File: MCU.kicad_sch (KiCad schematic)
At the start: 21 parts, among them U6 STM32F103RBTx, Y1 LFXTAL026380

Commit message: final version v2.1
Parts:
- C78, C79: value 100n -> 22p
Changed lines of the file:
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@@
       (effects (font (size 1.27 1.27)) (justify left))
     )
-    (property "Value" "100n" (id 1) (at 77.47 125.73 0)
+    (property "Value" "22p" (id 1) (at 77.47 125.73 0)
       (effects (font (size 1.27 1.27)) (justify left))
     )
@@
       (effects (font (size 1.27 1.27)) (justify left))
     )
-    (property "Value" "100n" (id 1) (at 93.98 125.73 0)
-      (effects (font (size 1.27 1.27)) (justify left))
-    )
+    (property "Value" "22p" (id 1) (at 93.98 125.73 0)
+      (effects (font (size 1.27 1.27)) (justify left))
+    )

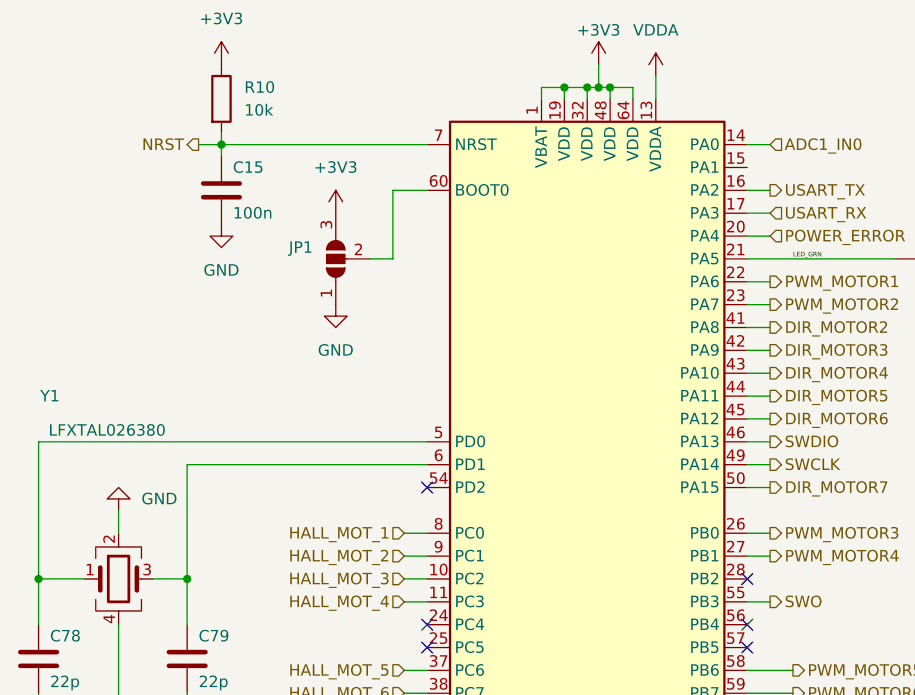
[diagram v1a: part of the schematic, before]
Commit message: updated footprints on board and sgematics
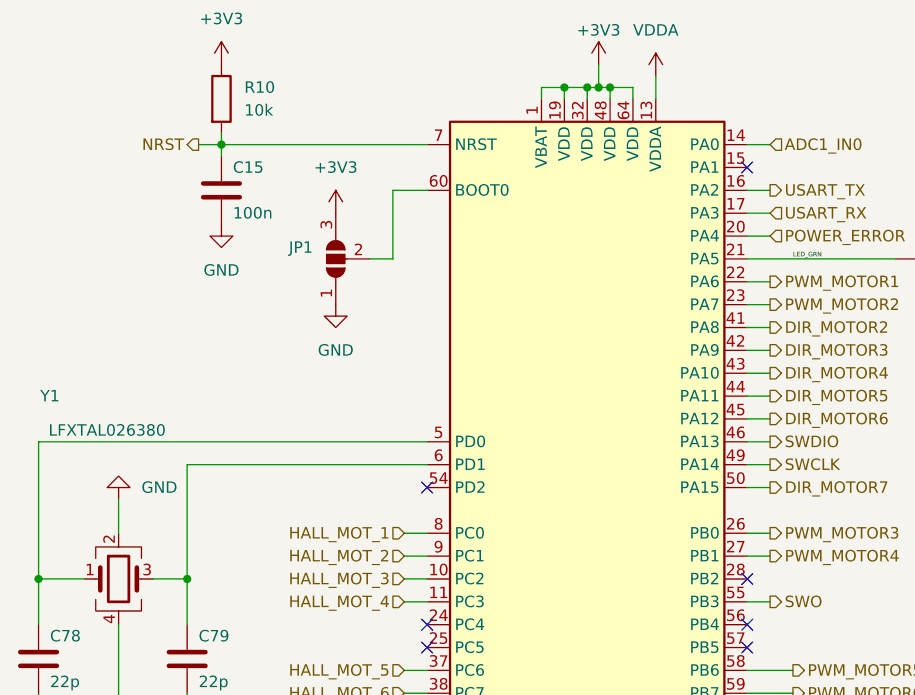
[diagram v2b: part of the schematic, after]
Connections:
- net VDDA: no longer names the net of C80.1, C81.1, FB1.2
- net VDDA: no longer U6.13 (VDDA)
- no-connect marks 13 -> 14
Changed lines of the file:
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@@
   (no_connect (at 154.94 121.92))
   (no_connect (at 154.94 132.08))
+  (no_connect (at 154.94 68.58))
   (no_connect (at 119.38 104.14))
   (wire (pts (xy 85.09 119.38) (xy 85.09 129.54))
@@
     (stroke (width 0) (type default) (color 0 0 0 0))
   )
-  (wire (pts (xy 85.09 106.68) (xy 85.09 109.22))
+  (wire (pts (xy 85.09 105.41) (xy 85.09 109.22))
     (stroke (width 0) (type default) (color 0 0 0 0))
   )
@@
     (pin "9")
   )
-  (symbol (lib_id "power:GND") (at 85.09 106.68 180) (unit 1)
-    (in_bom yes) (on_board yes) (fields_autoplaced)
-    (property "Reference" "#PWR030" (id 0) (at 85.09 100.33 0)
-      (effects (font (size 1.27 1.27)) hide)
-    )
-    (property "Value" "GND" (id 1) (at 87.63 105.4099 0)
+  (symbol (lib_id "power:GND") (at 85.09 105.41 180) (unit 1)
+    (in_bom yes) (on_board yes) (fields_autoplaced)
+    (property "Reference" "#PWR030" (id 0) (at 85.09 99.06 0)
+      (effects (font (size 1.27 1.27)) hide)
+    )
+    (property "Value" "GND" (id 1) (at 87.63 104.1399 0)
       (effects (font (size 1.27 1.27)) (justify right))
     )
-    (property "Footprint" "" (id 2) (at 85.09 106.68 0)
-      (effects (font (size 1.27 1.27)) hide)
-    )
-    (property "Datasheet" "" (id 3) (at 85.09 106.68 0)
+    (property "Footprint" "" (id 2) (at 85.09 105.41 0)
+      (effects (font (size 1.27 1.27)) hide)
+    )
+    (property "Datasheet" "" (id 3) (at 85.09 105.41 0)
       (effects (font (size 1.27 1.27)) hide)
     )
@@
     (pin "2")
   )
-  (symbol (lib_id "power:VDDA") (at 144.78 58.42 0) (unit 1)
+  (symbol (lib_name "VDDA_1") (lib_id "power:VDDA") (at 144.78 58.42 0) (unit 1)
     (in_bom yes) (on_board yes) (fields_autoplaced)
     (property "Reference" "#PWR0211" (id 0) (at 144.78 62.23 0)
